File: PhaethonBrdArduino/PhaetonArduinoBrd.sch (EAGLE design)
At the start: 25 parts, among them IC1 DS1307, Q1 32.768 Hz, SW1 EC12E_SW

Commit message: Schematic updated
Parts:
- removed U$1: DISCLAIMER, SmartPrj:DISCLAIMER
- added C2: 100nF, rcl:C-EUC0805K
- added C_INPUT: 330uF, resistor:CPOL-EU140CLH-1010
- added C_OUTPUT: 3.3nF, resistor:CPOL-EU140CLH-1010
- added D1: MBRS340T3, diode:MBRS340T3
- added IC2: LM2596T, national-semiconductor:LM2596T
- added L1: 68uH, rcl:L-EUL5038P
- added LED1: GM5WA94310A, led:GM5WA94310A
- added R10: 4K, SparkFun:RESISTOR
- added R11, R8: 10K\, SparkFun:RESISTOR
- added R9: 20K, SparkFun:RESISTOR
- added SJ1: (no value), jumper:SJ
- added SL1: (no value), con-amp-quick:M04
- added SV1: (no value), con-amp-mt6:MT6-3
- added T1: (no value), transistor:BC818-16-NPN-SOT23-BEC
- added U$2: ADT7301, analogLIB:ADT7301
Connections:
- net N$1 renamed PIN13
- net N$3 renamed PIN11
- net N$4 renamed PIN12
- net N$6 renamed PIN9
- net N$7 renamed PIN10
- net N$8 renamed PIN0
- removed net N$12: J1.5, J5.5
- removed net N$13: J1.6, J5.6
- removed net N$18: ANALOG.1, J6.1
- removed net N$19: ANALOG.2, J6.2
- removed net N$2: J3.1, J4.1
- removed net N$20: ANALOG.3, J6.3
- new net +24V: C_INPUT.+, IC2.VIN, R9.1, SV1-3.S
- new net A0: ANALOG.1, J6.1, LED1B.A
- new net A1: ANALOG.2, J6.2, LED1R.A
- new net A2: ANALOG.3, J6.3, LED1G.A
- new net N$1: D1.C, IC2.OUT, L1.2
- new net N$10: C_OUTPUT.+, IC2.FB, L1.1, SJ1.1
- new net N$11: LED1B.C, LED1G.C, LED1R.C, R11.2
- new net N$9: R10.1, R8.1, T1.B
- new net OUTPUT: R9.2, SV1-1.S, T1.C
- new net PIN1: J1.2, J5.2
- new net PIN5: J1.6, J5.6, U$2.CS
- new net PIN6: J1.7, J5.7, R10.2
- new net SCLK: U$2.SCLK
- net +5V: now also C2.1, SJ1.2, SL1.1, U$2.VDD
- net GND: now also C2.2, C_INPUT.-, C_OUTPUT.-, D1.A, IC2.!ON!/OFF, IC2.GND, R11.1, R8.2, SL1.2, SV1-2.S, T1.E, U$2.GND
- net MISO: now also U$2.DOUT
- net MOSI: now also U$2.DIN
- net PIN2: now also J1.3, J5.3; no longer J1.2, J5.2
- net PIN3: now also J1.4, J5.4; no longer J1.3, J5.3
- net PIN4: now also J1.5, J5.5; no longer J1.4, J5.4
- net PIN7: now also J1.8, J5.8, SL1.3; no longer J1.7, J5.7
- net PIN8: now also J3.1, J4.1, SL1.4; no longer J1.8, J5.8

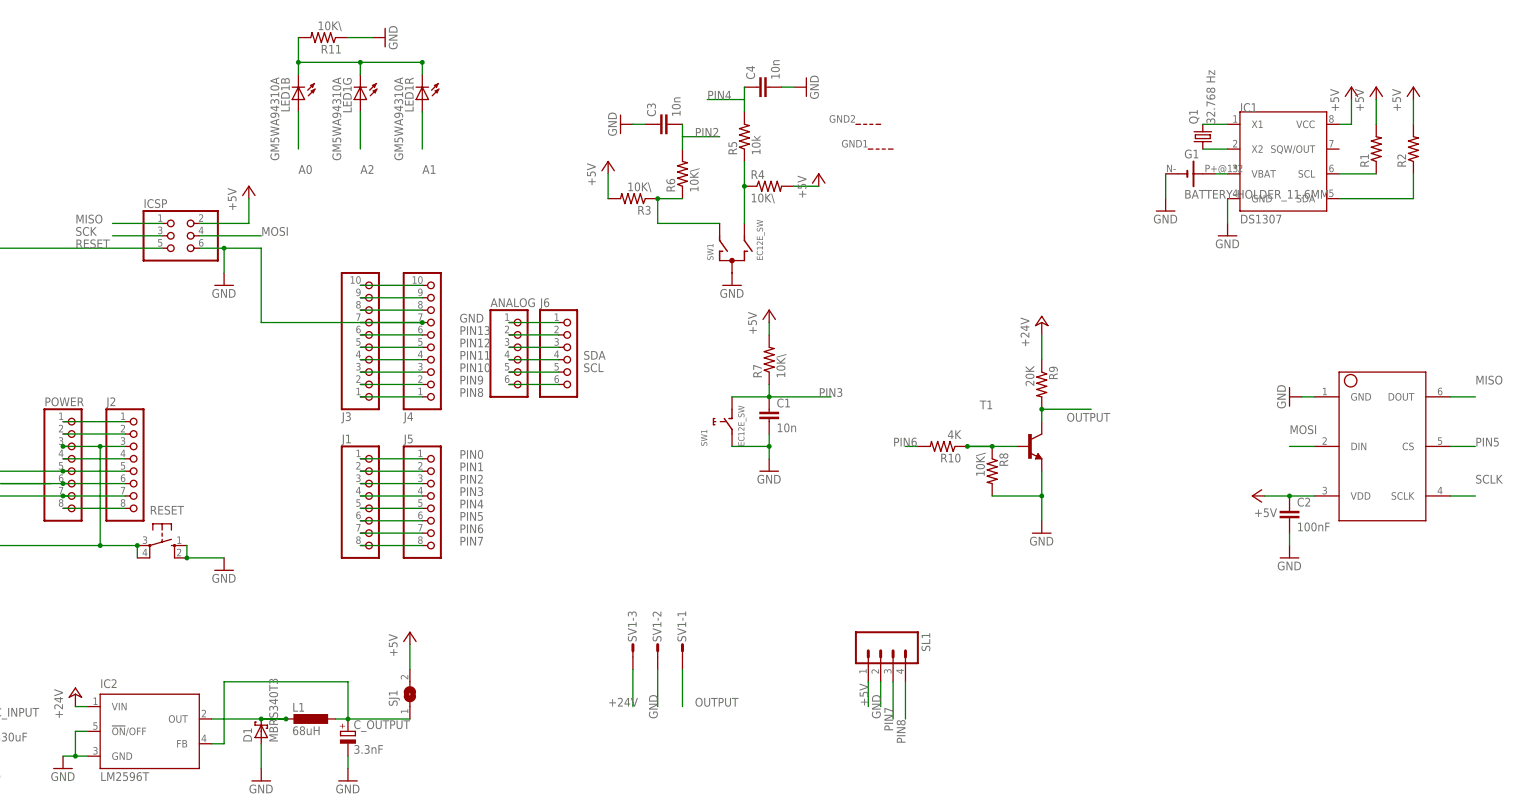
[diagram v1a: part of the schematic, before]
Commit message: added labels for every component
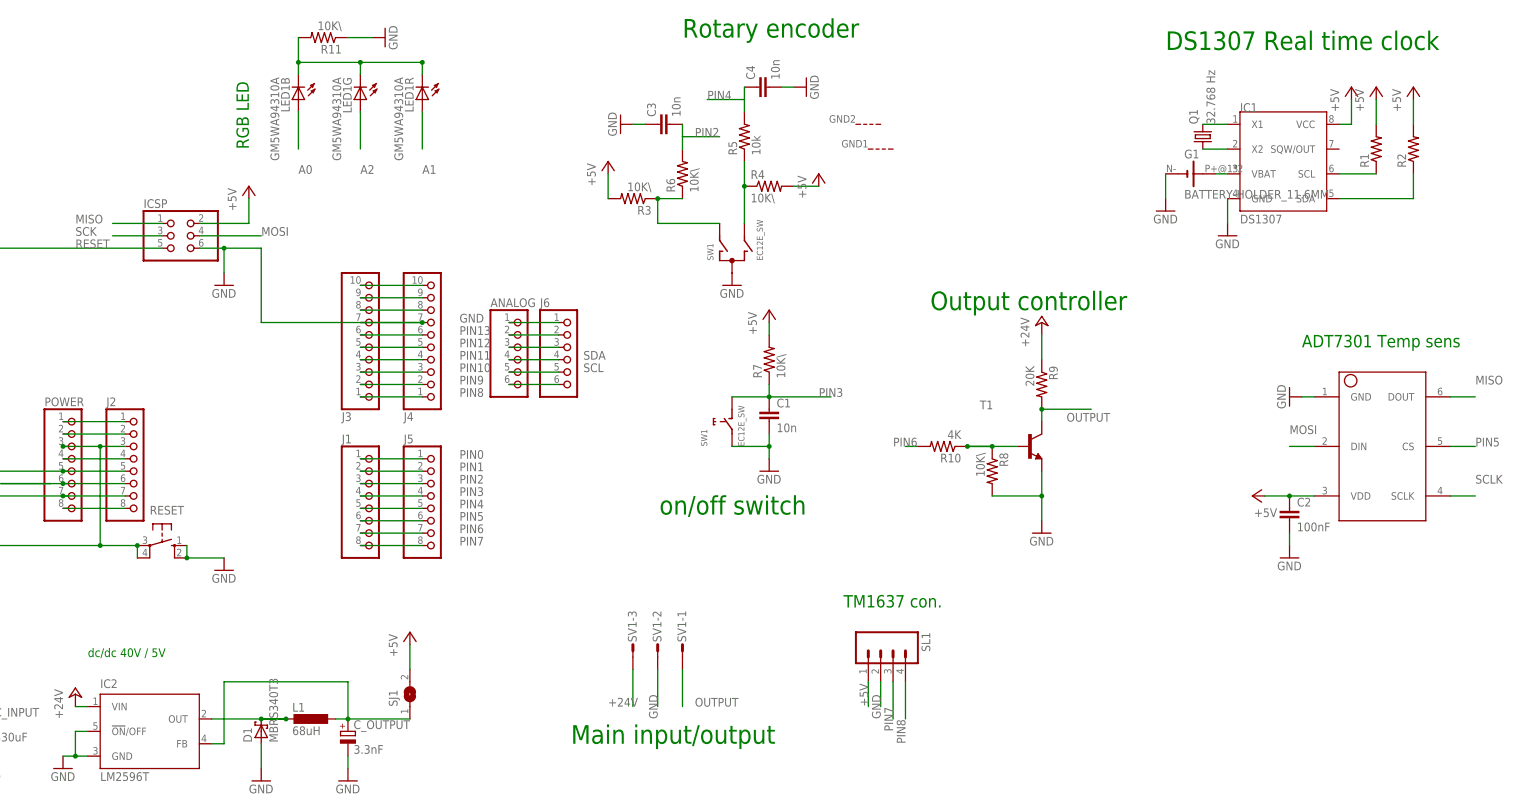
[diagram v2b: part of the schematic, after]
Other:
- note added: "ADT7301 Temp sens"
- note added: "DS1307 Real time clock"
- note added: "Main input/output"
- note added: "Output controller"
- note added: "RGB LED"
- note added: "Rotary encoder"
- note added: "TM1637 con."
- note added: "dc/dc 40V / 5V"
- note added: "on/off switch"
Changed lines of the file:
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@@
 <sheet>
 <plain>
+<text x="154.94" y="111.76" size="3.81" layer="91">Rotary encoder</text>
+<text x="254" y="109.22" size="3.81" layer="91">DS1307 Real time clock</text>
+<text x="66.04" y="88.9" size="2.54" layer="91" rot="R90">RGB LED</text>
+<text x="180.34" y="17.78" size="3.81" layer="91" rot="R180">on/off switch</text>
+<text x="132.08" y="-33.02" size="3.81" layer="91">Main input/output</text>
+<text x="187.96" y="-5.08" size="2.54" layer="91">TM1637 con.</text>
+<text x="205.74" y="55.88" size="3.81" layer="91">Output controller</text>
+<text x="281.94" y="48.26" size="2.54" layer="91">ADT7301 Temp sens</text>
+<text x="33.02" y="-15.24" size="1.778" layer="91">dc/dc 40V / 5V</text>
 </plain>
 <instances>
